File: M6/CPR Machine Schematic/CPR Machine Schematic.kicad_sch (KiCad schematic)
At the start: 0 parts

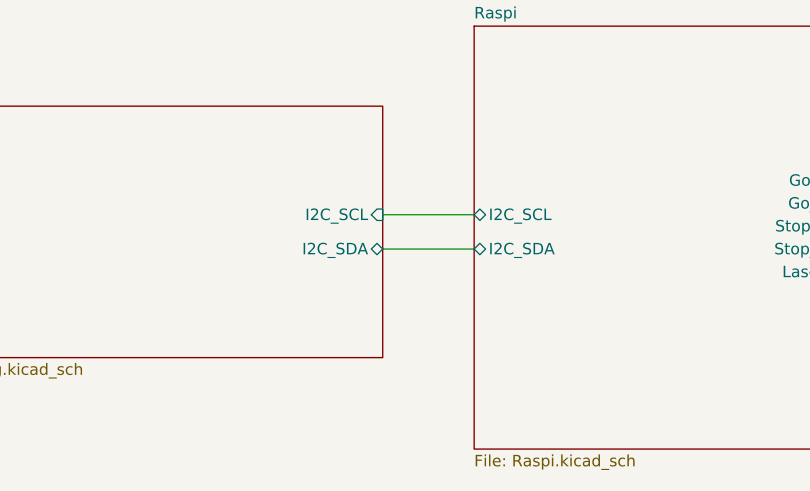
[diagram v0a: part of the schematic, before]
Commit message: Voltage readout, MUX, Debouncing Caps
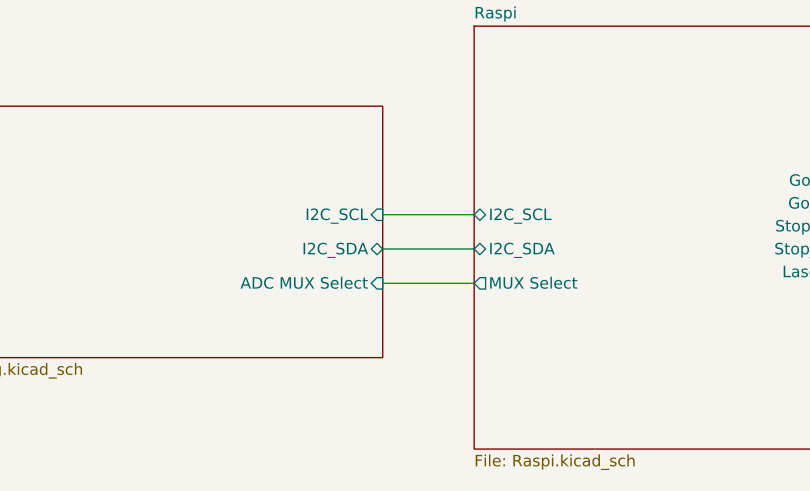
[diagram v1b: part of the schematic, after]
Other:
- sheet Raspi ports: added MUX Select; removed none
- sheet Sensing ports: added ADC MUX Select; removed none
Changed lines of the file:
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@@
+		)
+	)
+	(wire
+		(pts
+			(xy 110.49 87.63) (xy 120.65 87.63)
+		)
+		(stroke
+			(width 0)
+			(type default)
 		)
 	)
@@
 			)
 		)
+		(pin "ADC MUX Select" input
+			(at 110.49 87.63 0)
+			(effects
+				(font
+					(size 1.27 1.27)
+				)
+				(justify right)
+			)
+		)
 		(instances
 			(project "CPR Machine Schematic"
@@
 			)
 		)
+		(pin "MUX Select" output
+			(at 120.65 87.63 180)
+			(effects
+				(font
+					(size 1.27 1.27)
+				)
+				(justify left)
+			)
+		)
